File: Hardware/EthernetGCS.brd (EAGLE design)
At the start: 45.7 x 42.2 mm, 63 parts, among them IC3 24AA00OT, IC4 PIC24FJ64GA002_QFN, J2 HR911105A, Q2 25Mhz, U1 MIC5219-3.3V, U4 ENC28J60-QFN, U5 MIC5219-3.3V, U7 FT232RL-BASICSSOP, X2 USB-A-H

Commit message: Cleaning the schematic
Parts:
- removed C17: 10uF, rcl:SMC_A
- removed R10: 49R9 1%, SparkFun:0402-RES
- added C4: 0.1uF, SparkFun:0402-CAP
- added C5: 1uF, SparkFun:0402-CAP
- added R12: 49R9 1%, SparkFun:0402-RES
- added U3: MIC5219-3.3V, SparkFun:SOT23-5
- C15: value 0.1uF -> 470pF
- C16: value 0.1uF -> 10uF; device rcl:C0805 -> SparkFun:EIA3216
- moved C15 75.0 mm to (3.81, -56.5), turned to 0 degrees
- moved R8 72.3 mm to (0.64, -44.5), turned to 0 degrees
- moved R9 72.3 mm to (0.64, -38.1), turned to 0 degrees
- moved R7 71.4 mm to (0.64, -41.3), turned to 0 degrees
- moved C14 62.6 mm to (0.64, -34.9), turned to 0 degrees
- moved C16 46.6 mm to (1.91, -53.3), turned to 0 degrees
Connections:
- net N$10 renamed LED_TX
- net N$11 renamed LED_RX
- net SCL_1 renamed SCL
- net SDA_1 renamed SDA
- removed net ETH-INT: U4.28
- removed net ETH-RST: U4.6
- new net N$3: C15.1, U3.4
- net 3.3V: now also C16.A, U3.5
- net 5V: now also C5.1, U3.1, U3.3
- net CCT: now also C14.2, R12.1, R9.1; no longer C15.1, R10.2, R9.2
- net GND: now also C16.C, C4.2, C5.2, U3.2; no longer C16.2, C17.-
- net N$22: now also C4.1, R7.1, R8.1; no longer C14.2, R7.2, R8.2
- net RD+: now also R7.2; no longer R8.1
- net RD-: now also R8.2; no longer R7.1
- net TD+: now also R12.2; no longer R10.1
- net TD-: now also R9.2; no longer R9.1
- net V+: no longer C16.1, C17.+

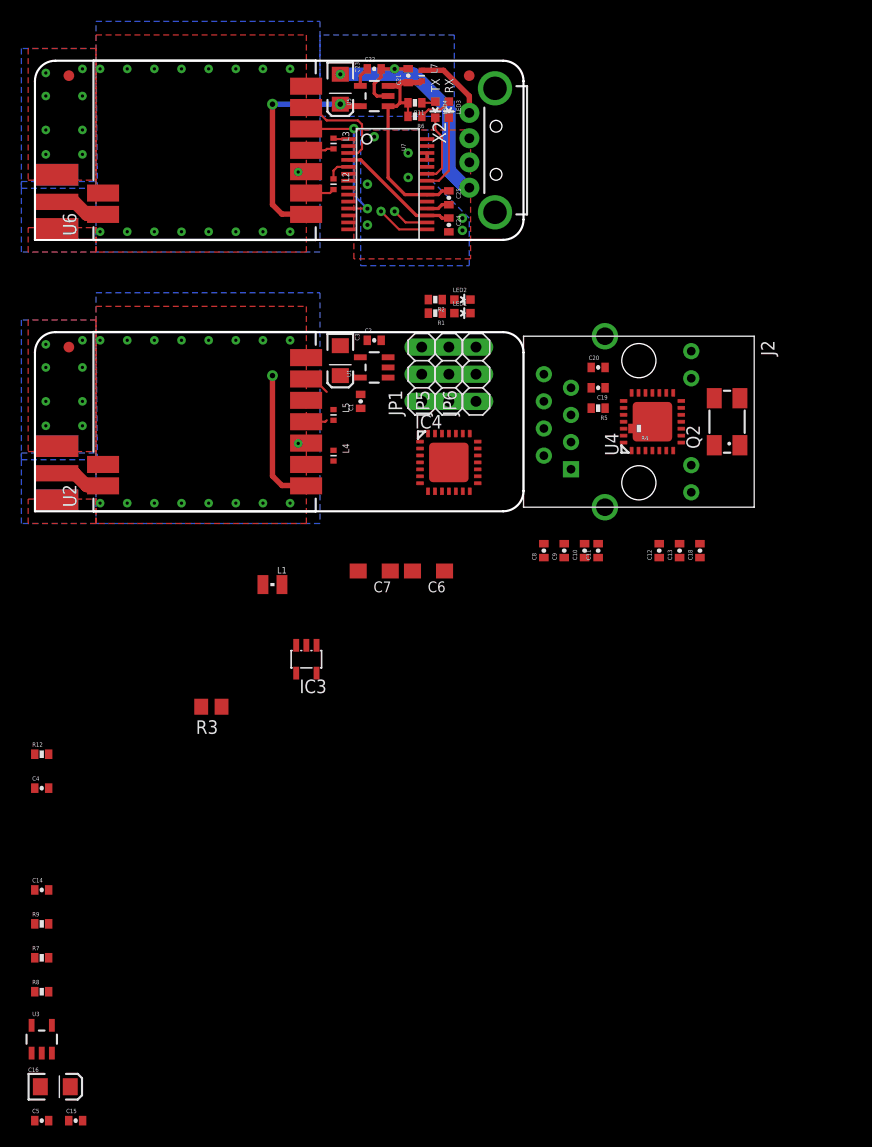
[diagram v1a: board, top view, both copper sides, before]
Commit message: Splitting the schematic into two sheets
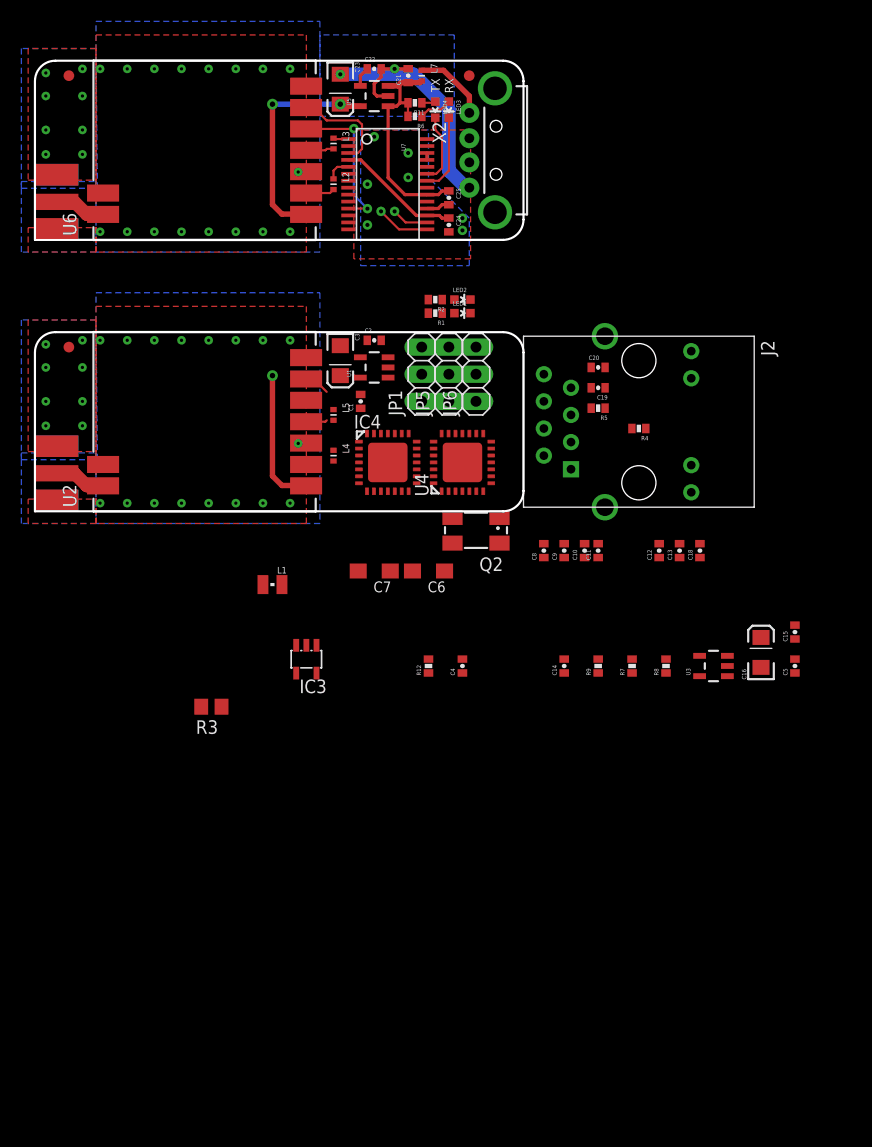
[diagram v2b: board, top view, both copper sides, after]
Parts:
- moved C5 82.3 mm to (71.1, -14.0), turned to 90 degrees
- moved C15 81.4 mm to (71.1, -10.8), turned to 90 degrees
- moved C16 77.5 mm to (67.9, -12.7), turned to 90 degrees
- moved U3 71.9 mm to (63.5, -14.0), turned to 90 degrees
- moved R8 65.9 mm to (59.1, -14.0), turned to 90 degrees
- moved R7 61.6 mm to (55.9, -14.0), turned to 90 degrees
- moved R9 57.4 mm to (52.7, -14.0), turned to 90 degrees
- moved C14 53.2 mm to (49.5, -14.0), turned to 90 degrees
- moved C4 41.0 mm to (40.0, -14.0), turned to 90 degrees
- moved R12 37.1 mm to (36.8, -14.0), turned to 90 degrees
- moved Q2 25.6 mm to (41.3, -1.27), turned to 180 degrees
- moved U4 18.2 mm to (40.0, 5.08)
- moved IC4 5.71 mm to (33.0, 5.08)

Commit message: Changing the RC connectors for the one in the SparkFun library
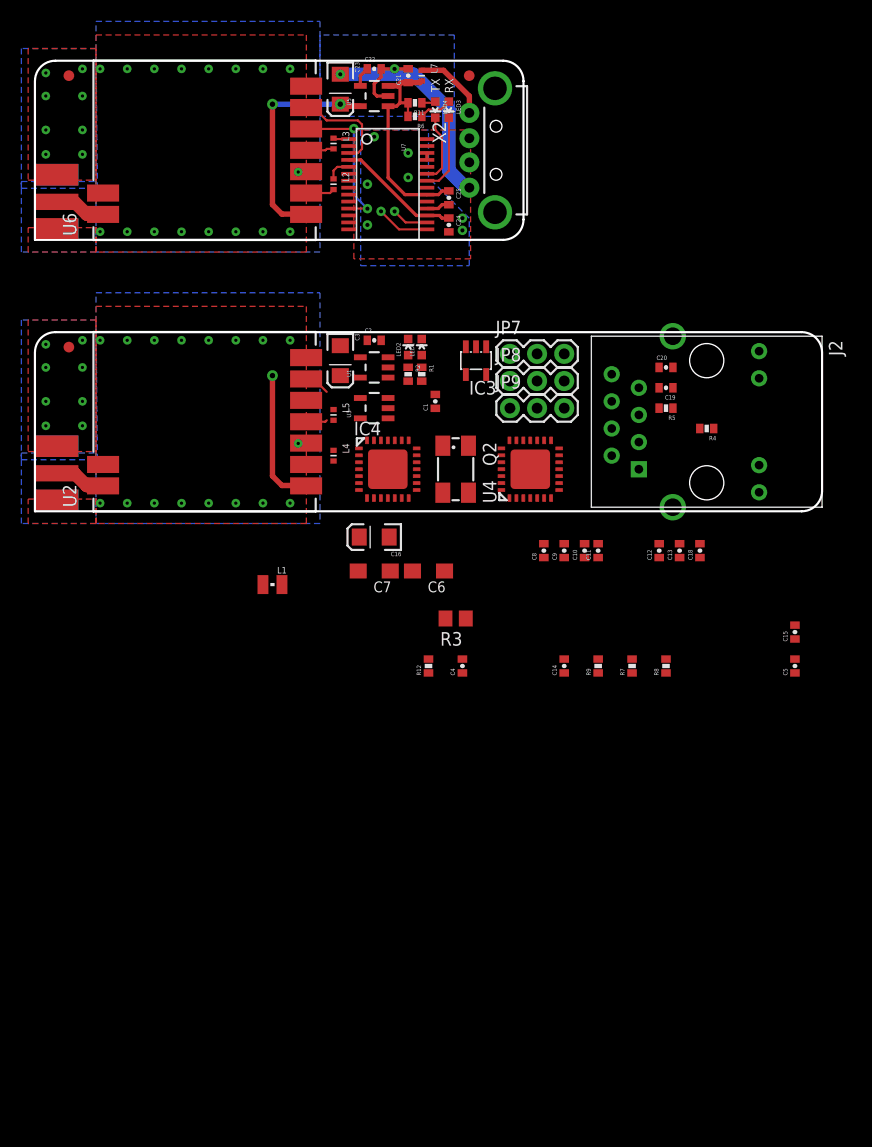
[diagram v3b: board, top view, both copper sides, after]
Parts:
- removed JP1, JP5, JP6: (no value), pinhead:1X03
- added JP7, JP8, JP9: (no value), SparkFun-Connectors:1X03
- moved U3 39.9 mm to (31.8, 10.2)
- moved C16 37.8 mm to (31.8, -1.91), turned to 180 degrees
- moved IC3 32.1 mm to (41.3, 14.6)
- moved R3 24.3 mm to (39.4, -9.53)
- moved R2 7.43 mm to (34.9, 13.3), turned to 270 degrees
- moved C1 6.99 mm to (37.5, 10.8)
- moved LED2 6.75 mm to (34.9, 15.9), turned to 0 degrees
- moved U4 6.38 mm to (46.4, 4.45)
- moved C19 6.35 mm to (59.1, 12.1)
- moved C20 6.35 mm to (59.1, 14.0)
- moved J2 6.35 mm to (62.9, 8.89)
- moved R4 6.35 mm to (62.9, 8.26)
- moved R5 6.35 mm to (59.1, 10.2)
- moved Q2 6.02 mm to (39.4, 4.45), turned to 270 degrees
- moved R1 5.85 mm to (36.2, 13.3), turned to 270 degrees
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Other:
- board size 45.7 x 42.2 mm -> 73.7 x 42.2 mm

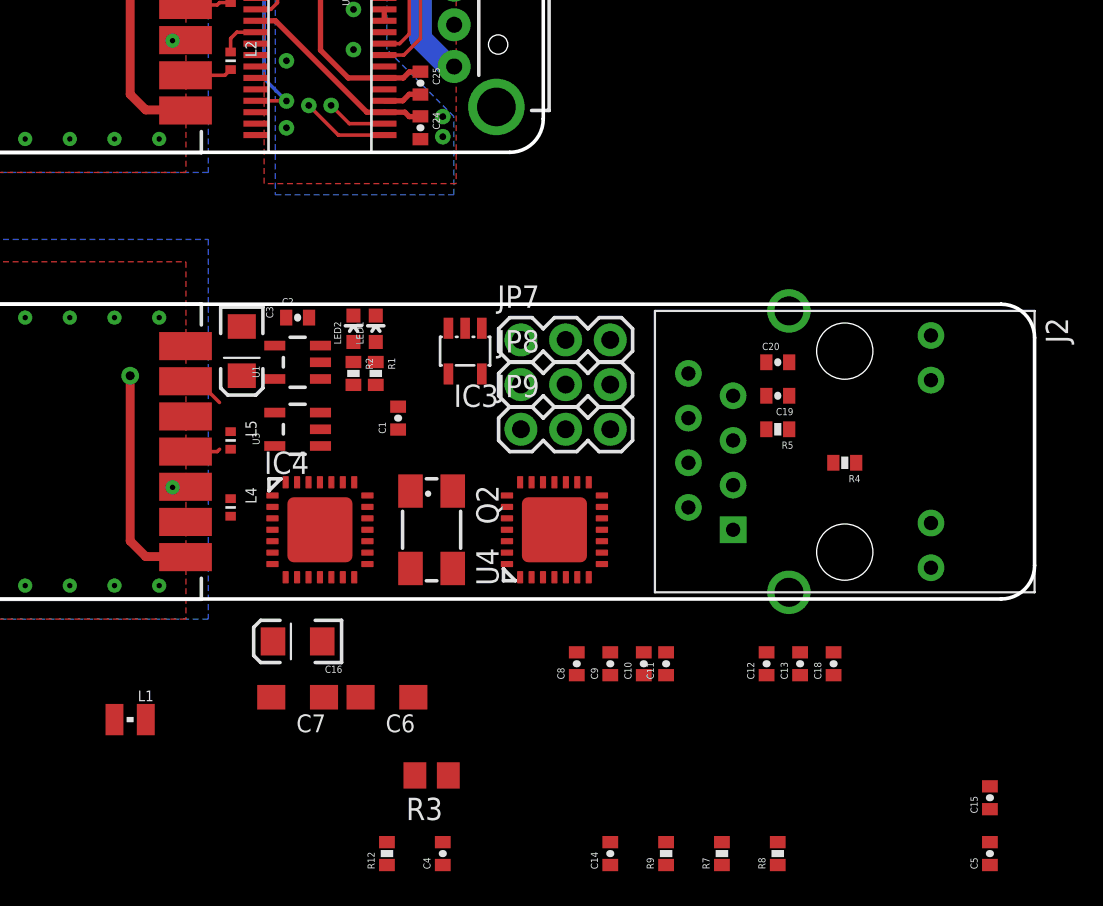
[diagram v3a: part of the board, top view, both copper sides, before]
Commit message: Adding information to the RC section
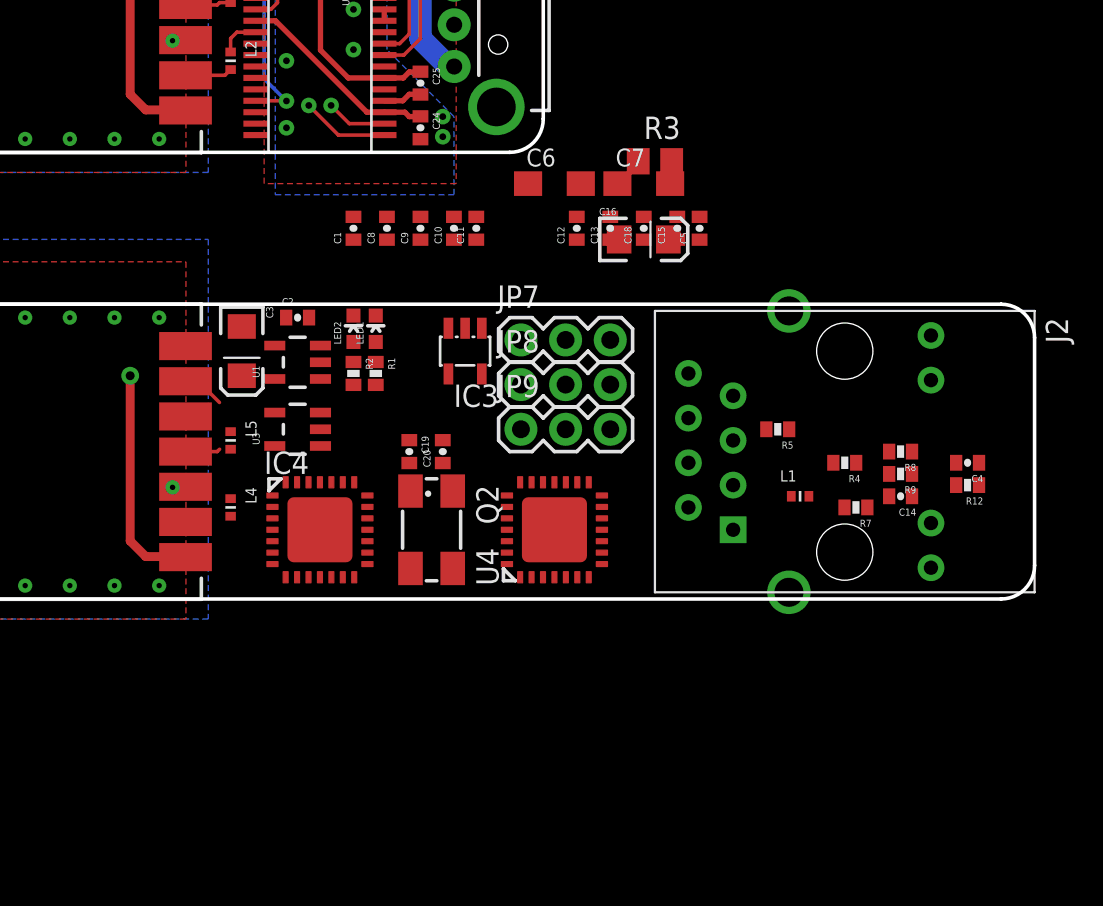
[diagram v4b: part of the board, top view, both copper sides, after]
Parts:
- L1: value (none) -> BLM15HD102SN1; device wuerth-elektronik:WE-KI_0805_B -> pel_dipol_comp:0402-IND
- moved L1 40.2 mm to (60.3, 6.35), turned to 0 degrees
- moved C5 39.2 mm to (54.6, 21.6)
- moved R12 39.1 mm to (69.8, 6.99), turned to 180 degrees
- moved C4 37.2 mm to (69.8, 8.26), turned to 180 degrees
- moved R3 37.2 mm to (52.1, 25.4), turned to 0 degrees
- moved C15 36.9 mm to (53.3, 21.6)
- moved C7 35.2 mm to (51.4, 24.1), turned to 0 degrees
- moved C6 30.7 mm to (46.4, 24.1), turned to 0 degrees
- moved C16 30.2 mm to (51.4, 21.0), turned to 0 degrees
- moved C10 27.0 mm to (40.6, 21.6)
- moved C11 27.0 mm to (41.9, 21.6)
- moved C12 27.0 mm to (47.6, 21.6)
- moved C13 27.0 mm to (49.5, 21.6)
- moved C18 27.0 mm to (51.4, 21.6)
- moved C8 27.0 mm to (36.8, 21.6)
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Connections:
- new net BAT_MON: JP7.3
- new net RC1: JP8.3
- new net RC2: JP9.3
- new net V_BAT: JP7.2, JP8.2, JP9.2
- net CCT: now also L1.P$1; no longer L1.2
- net GND: now also JP7.1, JP8.1, JP9.1
- net V+: now also L1.P$2; no longer L1.1

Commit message: Adding a sense line for the batterie
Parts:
- added R10, R13: (no value), SparkFun:0402-RES
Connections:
- removed net BAT_MON: JP7.3
- removed net N$16: C7.+
- new net BAT_SEN: R10.2, R13.2
- new net BAT_SEN1: JP7.3, R10.1
- net GND: now also R13.1; no longer C7.-
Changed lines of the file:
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@@
 <element name="JP9" library="SparkFun-Connectors" package="1X03" value="" x="44.45" y="10.16"/>
 <element name="L1" library="pel_dipol_comp" package="0402-IND" value="BLM15HD102SN1" x="60.325" y="6.35"/>
+<element name="R10" library="SparkFun" package="0402-RES" value="" x="0.635" y="-4.445"/>
+<element name="R13" library="SparkFun" package="0402-RES" value="" x="0.635" y="-7.62"/>
 </elements>
 <signals>
@@
 <contactref element="U4" pad="17"/>
 <contactref element="U4" pad="18"/>
-<contactref element="C7" pad="-"/>
 <contactref element="R3" pad="1"/>
 <contactref element="J2" pad="13"/>
@@
 <contactref element="JP8" pad="1"/>
 <contactref element="JP9" pad="1"/>
+<contactref element="R13" pad="1"/>
 <wire x1="69.2" y1="8.255" x2="67.7672" y2="12.954" width="0" layer="19" extent="1-1"/>
 <wire x1="66.69" y1="6.35" x2="69.2" y2="8.255" width="0" layer="19" extent="1-1"/>
@@
 <wire x1="47.625" y1="22.24" x2="49.53" y2="22.24" width="0" layer="19" extent="1-1"/>
 <wire x1="47.855" y1="24.13" x2="47.625" y2="22.24" width="0" layer="19" extent="1-1"/>
-<wire x1="52.935" y1="24.13" x2="53.34" y2="22.24" width="0" layer="19" extent="1-1"/>
-<wire x1="51.12" y1="25.4" x2="52.935" y2="24.13" width="0" layer="19" extent="1-1"/>
+<wire x1="51.12" y1="25.4" x2="51.435" y2="22.24" width="0" layer="19" extent="1-1"/>
 <wire x1="41.91" y1="22.24" x2="47.625" y2="22.24" width="0" layer="19" extent="1-1"/>
 <wire x1="40.64" y1="22.24" x2="41.91" y2="22.24" width="0" layer="19" extent="1-1"/>
@@
 <wire x1="43.655" y1="3.795" x2="46.355" y2="4.445" width="0" layer="19" extent="1-1"/>
 <wire x1="48.305" y1="1.745" x2="46.355" y2="4.445" width="0" layer="19" extent="1-1"/>
+<wire x1="-0.015" y1="-7.62" x2="2.032" y2="1.524" width="0" layer="19" extent="1-16"/>
 </signal>
 <signal name="N$2">
@@
 <wire x1="40.57" y1="2.245" x2="40.005" y2="8.24" width="0" layer="19" extent="1-1"/>
 </signal>
-<signal name="N$16">
-<contactref element="C7" pad="+"/>
-</signal>
 <signal name="N$22">
 <contactref element="C4" pad="1"/>
@@
 <wire x1="46.99" y1="10.16" x2="46.99" y2="12.7" width="0" layer="19" extent="1-1"/>
 </signal>
-<signal name="BAT_MON">
+<signal name="BAT_SEN1">
 <contactref element="JP7" pad="3"/>
+<contactref element="R10" pad="1"/>
+<wire x1="-0.015" y1="-4.445" x2="49.53" y2="15.24" width="0" layer="19" extent="1-1"/>
 </signal>
 <signal name="RC1">
@@
 <contactref element="JP9" pad="3"/>
 </signal>
+<signal name="BAT_SEN">
+<contactref element="R13" pad="2"/>
+<contactref element="R10" pad="2"/>
+<wire x1="1.285" y1="-4.445" x2="1.285" y2="-7.62" width="0" layer="19" extent="1-1"/>
+</signal>
 </signals>

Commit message: Just moving some parts to easy  layout process.
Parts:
- moved R13 55.9 mm to (48.3, 21.6), turned to 270 degrees
- moved R10 55.4 mm to (49.5, 21.6), turned to 270 degrees
- moved C5 15.2 mm to (39.4, 21.6)
- moved C7 8.25 mm to (59.1, 21.0), turned to 90 degrees
- moved C20 6.84 mm to (42.5, 2.54)
- moved C15 6.35 mm to (47.0, 21.6)
- moved R3 6.29 mm to (56.5, 21.0), turned to 270 degrees
- moved C6 5.99 mm to (51.4, 21.0), turned to 90 degrees
- moved C18 5.72 mm to (45.7, 21.6)
- moved C19 5.12 mm to (42.5, 6.35)
- moved C13 5.08 mm to (44.5, 21.6)
- moved C12 4.45 mm to (43.2, 21.6)
- moved C16 2.54 mm to (54.0, 21.0), turned to 270 degrees
- moved C1 0.64 mm to (35.6, 21.6)
- moved U4 0.64 mm to (47.0, 4.45)
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
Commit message: Connecting the power pins of the uC.
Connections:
- removed net VDD: IC4.10, IC4.25
- removed net VDDCORE: IC4.17
- new net N$5: C7.+, IC4.17
- net 3.3V: now also IC4.10, IC4.25
- net GND: now also C7.-, IC4.16, IC4.24
- net VSS: no longer IC4.24
